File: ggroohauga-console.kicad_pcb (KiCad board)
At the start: 2 copper layers, 85.3 x 31 mm, 4 parts

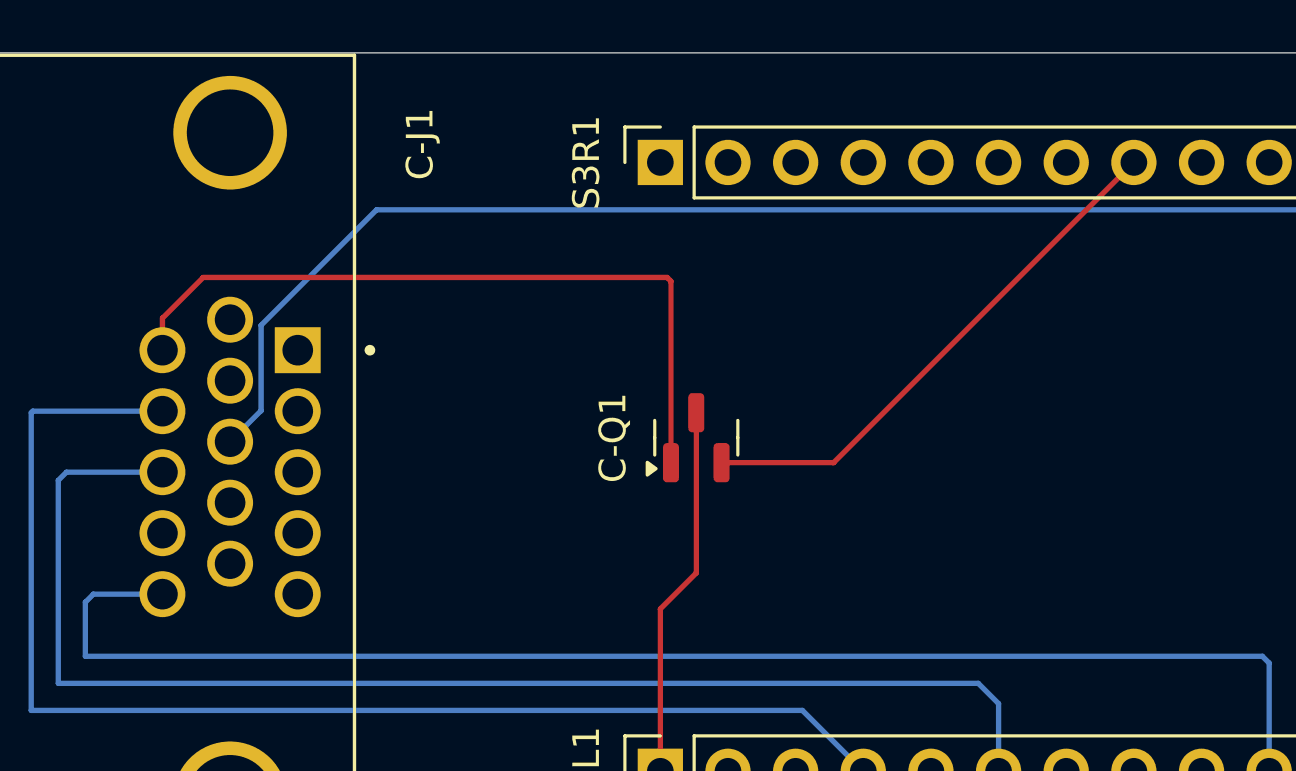
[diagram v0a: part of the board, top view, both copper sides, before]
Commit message: Rotate MOSFET pins so that it's connected correctly
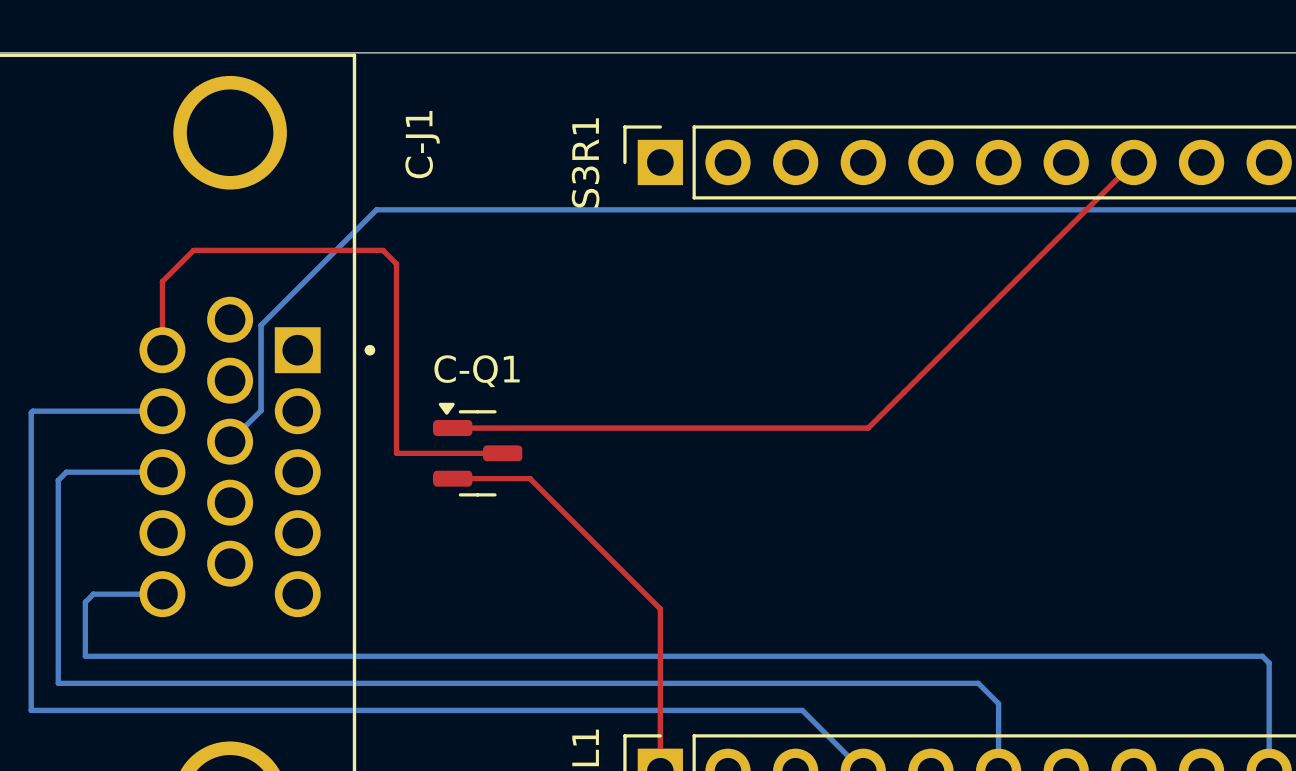
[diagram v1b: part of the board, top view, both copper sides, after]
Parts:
- moved C-Q1 8.23 mm to (74.7, 65.5), turned to 0 degrees
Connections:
- C-J1 pad 1: unconnected-(C-J1-Pad1) -> AUDIO_HEADPHONES_R
- C-J1 pad 2: unconnected-(C-J1-Pad2) -> AUDIO_HEADPHONES_L
- C-J1 pad 3: unconnected-(C-J1-Pad3) -> AUDIO_GROUND
- C-J1 pad 4: unconnected-(C-J1-Pad4) -> AUDIO_AUX_R
- C-J1 pad 5: unconnected-(C-J1-Pad5) -> AUDIO_AUX_L
- C-Q1 pad 1: /CON_POWER_OUT -> /GPIO_L40_C40_M41/CON_POWER_OUT
- C-Q1 pad 2: /GPIO_L40_C40_M41/CON_POWER_OUT -> +3.3V
- C-Q1 pad 3: +3.3V -> /CON_POWER_OUT
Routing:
- net /GPIO_L40_C40_M41/CON_POWER_OUT: track 20.2 -> 29.7 mm
- net /CON_POWER_OUT: track 27.8 -> 23.2 mm
- net +3.3V: track 14.2 -> 16.1 mm

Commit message: Fix console oid
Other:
- board text added: "urn:oid:1.3.6.1.4.1.39777.1.3.1.2.1 https://github.com/nomis/ggroohauga-pcb (console)"
- board text removed: "urn:oid:1.3.6.1.4.1.39777.1.3.1.1.1 https://github.com/nomis/ggroohauga-pcb (console)"
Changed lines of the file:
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@@
 		)
 	)
-	(gr_text "urn:oid:1.3.6.1.4.1.39777.1.3.1.1.1\nhttps://github.com/nomis/ggroohauga-pcb\n(console)"
+	(gr_text "urn:oid:1.3.6.1.4.1.39777.1.3.1.2.1\nhttps://github.com/nomis/ggroohauga-pcb\n(console)"
 		(at 131.064 66.04 0)
 		(layer "B.SilkS")

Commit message: Cleanup tracks
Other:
- board text added: "urn:oid:1.3.6.1.4.1.39777.1.3.1.2.2 https://github.com/nomis/ggroohauga-pcb (console)"
- board text removed: "urn:oid:1.3.6.1.4.1.39777.1.3.1.2.1 https://github.com/nomis/ggroohauga-pcb (console)"
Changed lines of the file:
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@@
 		)
 	)
-	(gr_text "urn:oid:1.3.6.1.4.1.39777.1.3.1.2.1\nhttps://github.com/nomis/ggroohauga-pcb\n(console)"
+	(gr_text "urn:oid:1.3.6.1.4.1.39777.1.3.1.2.2\nhttps://github.com/nomis/ggroohauga-pcb\n(console)"
 		(at 131.064 66.04 0)
 		(layer "B.SilkS")
@@
 	)
 	(segment
-		(start 89.154 77.47)
-		(end 89.408 77.216)
-		(width 0.2)
-		(layer "F.Cu")
-		(net 15)
-	)
-	(segment
 		(start 57.9708 63.9492)
 		(end 62.8396 63.9492)
@@
 	(segment
 		(start 81.534 77.47)
-		(end 81.691 77.47)
-		(width 0.2)
-		(layer "F.Cu")
-		(net 18)
-	)
-	(segment
-		(start 81.534 77.47)
 		(end 81.534 71.374)
 		(width 0.2)
@@
 	)
 	(segment
-		(start 90.678 63.246)
+		(start 89.342 64.582)
 		(end 99.314 54.61)
 		(width 0.2)
 		(layer "F.Cu")
-		(net 19)
-	)
-	(segment
-		(start 89.342 64.582)
-		(end 90.678 63.246)
-		(width 0.2)
-		(layer "F.Cu")

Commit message: Convert to KiCad 9.0 format
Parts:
- C-J1: value DE15_Plug_HighDensity_MountingHoles -> DE15_Pins_HighDensity_MountingHoles

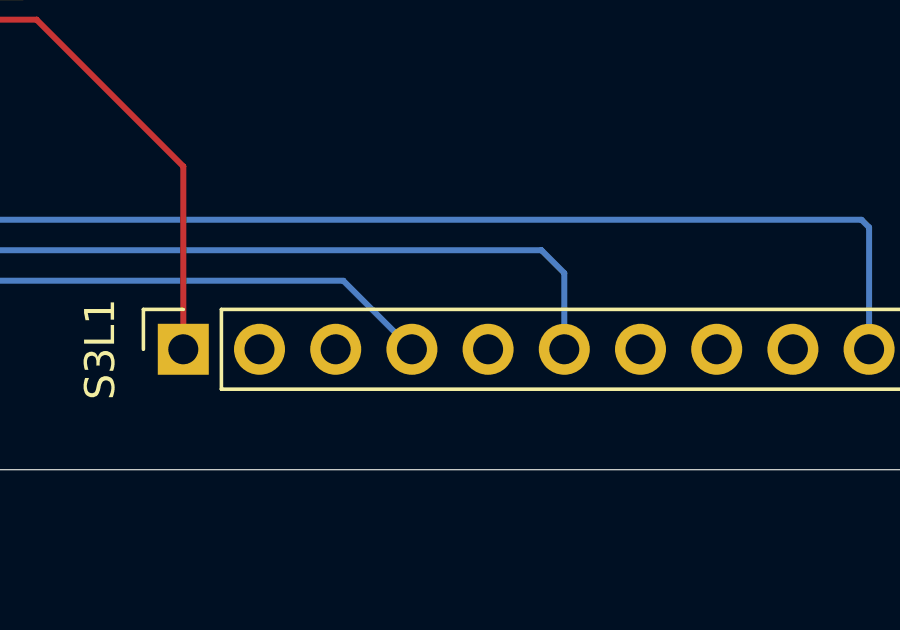
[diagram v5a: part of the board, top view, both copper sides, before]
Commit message: Reorganise schematic into multiple sheets and add 3 board identifier GPIOs
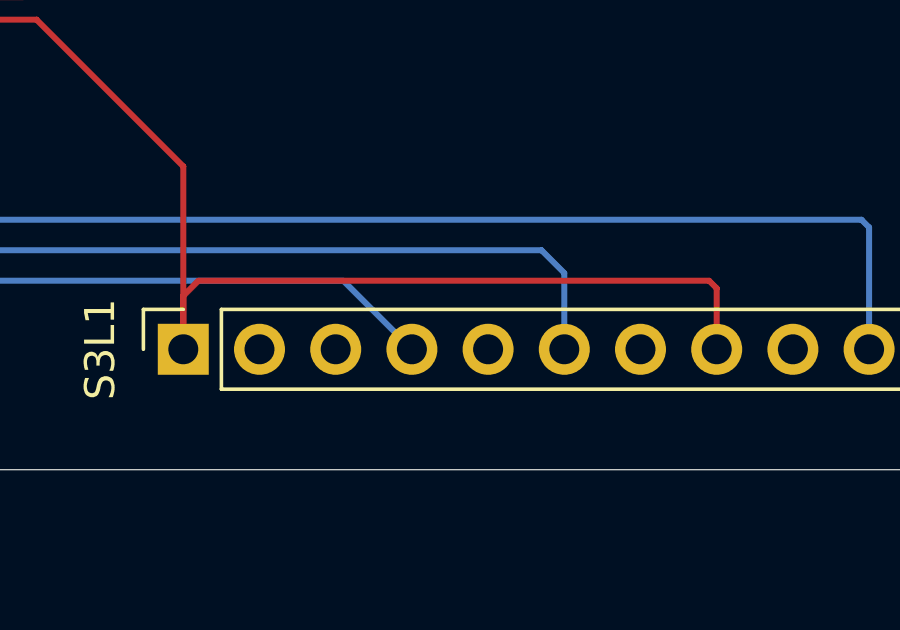
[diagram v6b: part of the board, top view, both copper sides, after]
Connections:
- net /CON_POWER_OUT renamed /Common/CON_POWER_OUT
- net /GPIO_L10_C10_M14/AMP_RX renamed /Common/GPIO_L10_C10_M14/AMP_RX
- net /GPIO_L13_C47_M26/AMP_ANNOUNCE renamed /Common/GPIO_L13_C47_M26/AMP_ANNOUNCE
- net /GPIO_L14_C48_M33/AMP_DETECT renamed /Common/GPIO_L14_C48_M33/AMP_DETECT
- net /GPIO_L17_C17_M8/CON_DETECT renamed /Common/GPIO_L17_C17_M8/CON_DETECT
- net /GPIO_L40_C40_M41/CON_POWER_OUT renamed /Common/GPIO_L40_C40_M41/CON_POWER_OUT
- net /GPIO_L48_C35_M36/CON_ANNOUNCE renamed /Common/GPIO_L48_C35_M36/CON_ANNOUNCE
- net /GPIO_L4_C4_M2/CON_RX renamed /Common/GPIO_L4_C4_M2/CON_RX
- net /GPIO_L6_C6_M4/CON_TX renamed /Common/GPIO_L6_C6_M4/CON_TX
- net /GPIO_L8_C8_M10/AMP_POWER_IN renamed /Common/GPIO_L8_C8_M10/AMP_POWER_IN
- net /GPIO_L9_C9_M13/AMP_TX renamed /Common/GPIO_L9_C9_M13/AMP_TX
- S3L1 pad 11: unconnected-(S3L1-Pin_11-Pad11) -> GPIO_L18_C18_M9
- S3L1 pad 17: unconnected-(S3L1-Pin_17-Pad17) -> GPIO_L11_C11_M15
- S3L1 pad 18: unconnected-(S3L1-Pin_18-Pad18) -> GPIO_L12_C12_M16
- S3L1 pad 7: unconnected-(S3L1-Pin_7-Pad7) -> GND
- S3L1 pad 8: unconnected-(S3L1-Pin_8-Pad8) -> +3.3V
- S3L1 pad 9: unconnected-(S3L1-Pin_9-Pad9) -> GND
- S3R1 pad 14: unconnected-(S3R1-Pin_14-Pad14) -> GPIO_L47_C47_M35
- S3R1 pad 15: unconnected-(S3R1-Pin_15-Pad15) -> GPIO_L21_C21_M21
- S3R1 pad 7: unconnected-(S3R1-Pin_7-Pad7) -> GPIO_L41_C41_M42
- S3R1 pad 9: unconnected-(S3R1-Pin_9-Pad9) -> GPIO_L39_C39_M40
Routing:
- net +3.3V: track 15.9 -> 37.8 mm
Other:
- board text added: "urn:oid:1.3.6.1.4.1.39777.1.3.1.2.3 https://github.com/nomis/ggroohauga-pcb (console)"
- board text removed: "urn:oid:1.3.6.1.4.1.39777.1.3.1.2.2 https://github.com/nomis/ggroohauga-pcb (console)"

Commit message: Ground unused GPIOs
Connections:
- C-J1 pad 0: GND -> GPIO_L11_C11_M15
- C-J1 pad 6: GND -> GPIO_L11_C11_M15
- S3L1 pad 11: GPIO_L18_C18_M9 -> GPIO_L11_C11_M15
- S3L1 pad 18: GPIO_L12_C12_M16 -> GPIO_L11_C11_M15
- S3L1 pad 7: GND -> GPIO_L11_C11_M15
- S3L1 pad 9: GND -> GPIO_L11_C11_M15
- S3R1 pad 1: GND -> GPIO_L11_C11_M15
- S3R1 pad 14: GPIO_L47_C47_M35 -> GPIO_L11_C11_M15
- S3R1 pad 15: GPIO_L21_C21_M21 -> GPIO_L11_C11_M15
- S3R1 pad 7: GPIO_L41_C41_M42 -> GPIO_L11_C11_M15
- S3R1 pad 9: GPIO_L39_C39_M40 -> GPIO_L11_C11_M15
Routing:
- added copper zone on B.Cu, net GPIO_L11_C11_M15
- added copper zone on F.Cu, net GPIO_L11_C11_M15
- removed copper zone on B.Cu, net GND
- removed copper zone on F.Cu, net GND
